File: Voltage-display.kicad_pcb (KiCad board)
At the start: 2 copper layers, 36 parts, among them IC1 TC7107ACPL, J1 Conn_01x02, J2 Conn_01x02, U1 AMC1311BQDWVQ1, U2 R05CT05S-R, U3 TC7660SEPA, U4 ADR510ARTZ-REEL7

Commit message: Update KiCad PCB
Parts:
- moved C7 27.3 mm to (128.4, 80.0)
- moved C6 25.1 mm to (128.5, 77.5)
- moved C9 23.1 mm to (146.5, 81.5), turned to 0 degrees
- moved C8 21.6 mm to (146.5, 78.0), turned to 90 degrees
- moved RV1 21.3 mm to (157.0, 101.5), turned to 90 degrees
- moved C2 15.4 mm to (127.5, 87.5)
- moved C3 14.4 mm to (127.5, 85.5)
- moved C5 10.8 mm to (146.5, 84.0), turned to 0 degrees
- moved C10 9.92 mm to (192.0, 72.9), turned to -90 degrees
- moved R5 7.52 mm to (155.0, 112.0), turned to -90 degrees
- moved R6 7.50 mm to (152.0, 107.5), turned to -90 degrees
- moved C1 7.43 mm to (127.5, 89.5)
- moved R4 7.37 mm to (127.5, 95.5)
- moved AFF3 6.34 mm to (210.0, 105.0)
- moved U1 6.31 mm to (137.4, 88.0)
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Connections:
- R5 pad 2: /TC7107_Display/VREF_1V -> Net-(U4-V+)
- U4 pad 1: /TC7107_Display/VREF_1V -> Net-(U4-V+)
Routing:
- net GND: track 169.6 -> 0.00 mm, vias 4 -> 0
- net /HV-: track 69.1 -> 3.63 mm, vias 5 -> 0
- net /TC7107_Display/VREF_1V: track 30.9 -> 4.55 mm
- net +5V: track 258.9 -> 282.7 mm, vias 8 -> 0
- net /TC7107_Display/F2: track 60.8 -> 41.3 mm, vias 1 -> 3
- net /TC7107_Display/E2: track 68.7 -> 50.0 mm, vias 2 -> 1
- net /ISO_5V: track 38.5 -> 19.8 mm, vias 2 -> 0
- net Net-(U3-CAP+): track 18.5 -> 3.22 mm
- net /HV_SENSE: track 21.8 -> 14.8 mm
- net /TC7107_Display/C2: track 65.5 -> 59.1 mm
- net /TC7107_Display/D2: track 53.8 -> 47.3 mm
- net Net-(U3-CAP-): track 7.58 -> 2.97 mm
- net /TC7107_Display/OSC1: track 10.6 -> 6.16 mm
- net /TC7107_Display/A3: track 55.2 -> 51.0 mm
- net /TC7107_Display/OSC3: track 13.4 -> 9.83 mm, vias 2 -> 0
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- added copper zone on F.Cu, net /HV-
- added copper zone on F.Cu, net GND

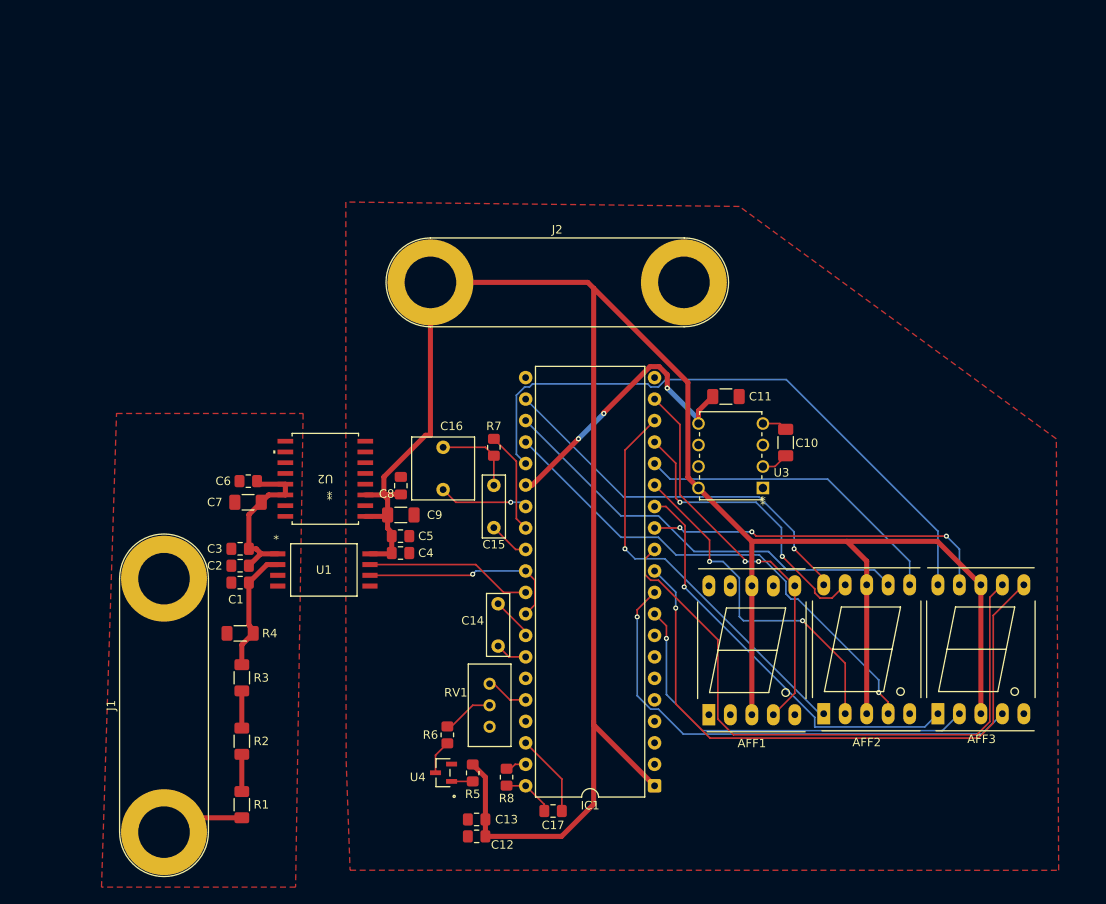
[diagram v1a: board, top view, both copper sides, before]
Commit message: Updated with Safety/Protection features
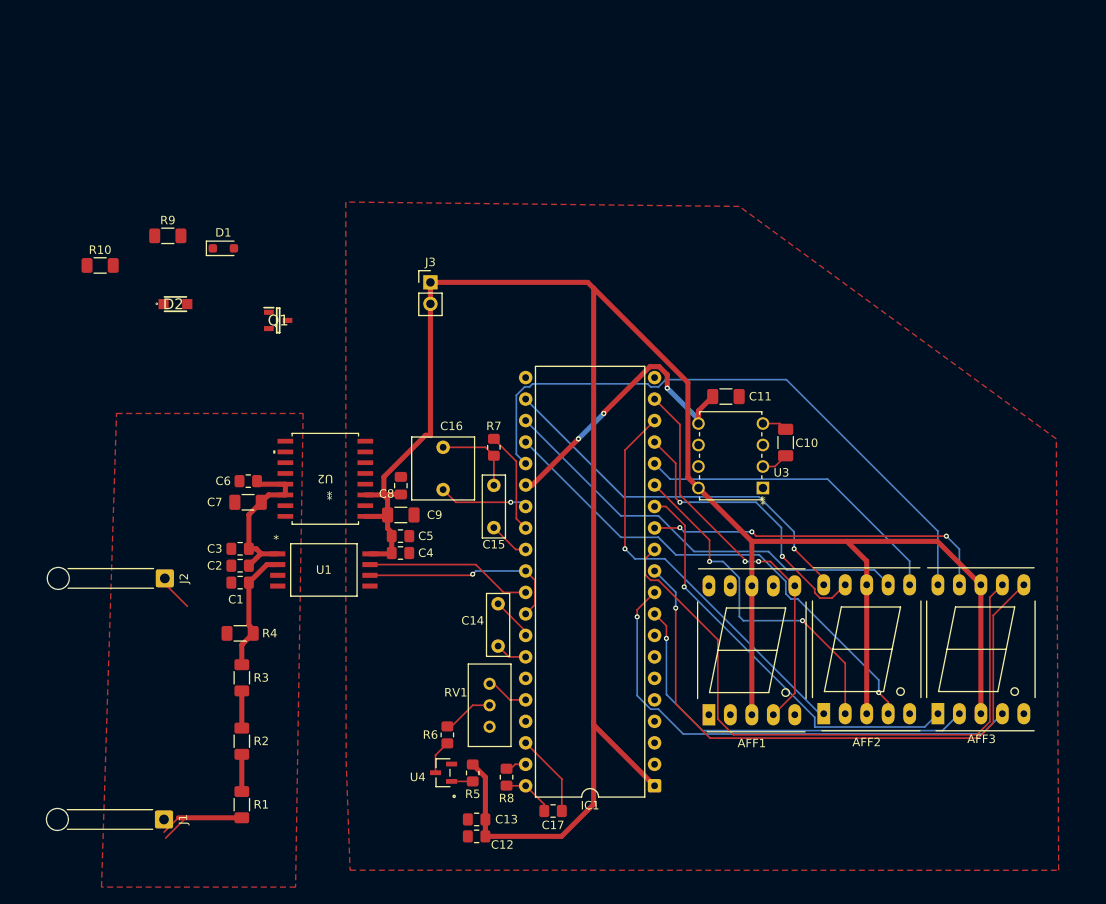
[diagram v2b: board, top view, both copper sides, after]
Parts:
- added D1: BZX38450-B2V2-Q, Diode_SMD:D_SOD-323_HandSoldering, F.Cu at (125.5, 50.0)
- added D2: PTVS5V0S1UR-Q, Voltage_Display_Footprints:SOD123W, F.Cu at (119.9, 56.6)
- added J2: HV- SOLDER, Connector_Wire:SolderWire-0.5sqmm_1x01_D0.9mm_OD2.1mm_Relief, F.Cu at (118.6, 89.0)
- added Q1: DMP2035UQ-7, Voltage_Display_Footprints:SOT96P240X115-3N, F.Cu at (132.0, 58.5)
- added R10: 100k, Resistor_SMD:R_1206_3216Metric_Pad1.30x1.75mm_HandSolder, F.Cu at (111.0, 52.0)
- added R9: 10k, Resistor_SMD:R_1206_3216Metric_Pad1.30x1.75mm_HandSolder, F.Cu at (119.0, 48.5)
- J1: value Conn_01x02 -> HV+ SOLDER; footprint Connector:Banana_Jack_2Pin -> Connector_Wire:SolderWire-0.5sqmm_1x01_D0.9mm_OD2.1mm_Relief
- J3: renamed from J2; footprint Connector:Banana_Jack_2Pin -> Connector_PinHeader_2.54mm:PinHeader_1x02_P2.54mm_Vertical
- moved J1 1.50 mm to (118.5, 117.5), turned to -90 degrees
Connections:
- J3 pad 1: +5V -> /+5V_IN
- U1 pad 2: /HV_SENSE -> Net-(U1-VIN)

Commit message: Added the switch for the votlage display
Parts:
- added RV2: 500, Potentiometer_THT:Potentiometer_Bourns_3296W_Vertical, F.Cu at (108.6, 62.2)
- R1, R2, R3: value 1M -> 100k
- R4: value 30.3k -> 2.8k
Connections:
- R4 pad 2: /HV- -> Net-(R4-Pad2)
